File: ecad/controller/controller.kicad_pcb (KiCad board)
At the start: 2 copper layers, 48 x 30 mm, 43 parts, among them J2 USB_C_Receptacle_PowerOnly_6P, SW1 SW, SW2 SW, SW3 SW, U1 ESP32-S3-WROOM-1, U2 AMS1117-3.3, U3 SN74LVC1T45DBV, U4 USBLC6-2SC6

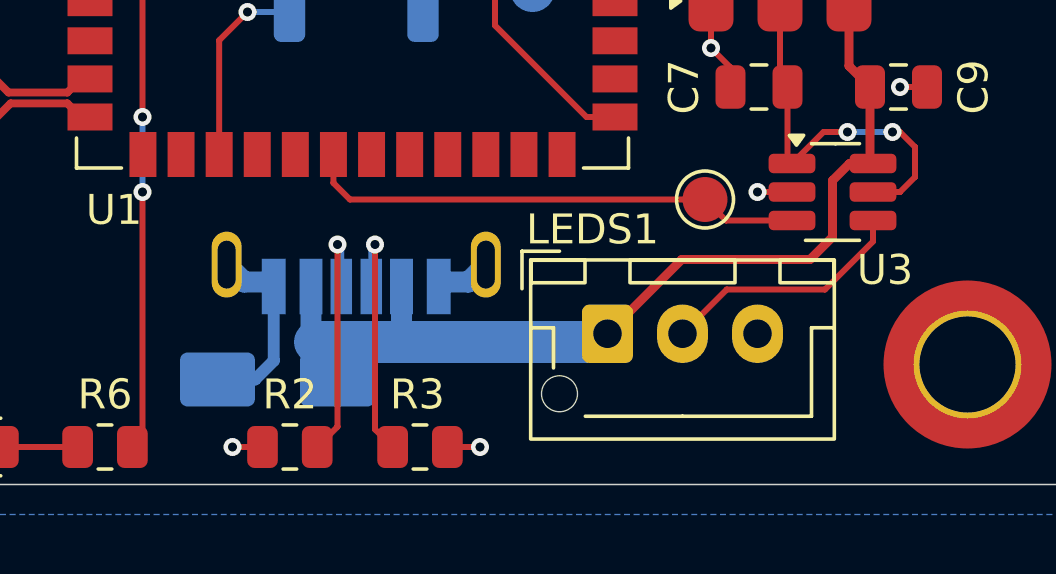
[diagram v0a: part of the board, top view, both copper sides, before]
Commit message: first controller board test complete! updated USB-C connector footprint as that was the only issue found so far
longer pads should make it easier to solder by giving the iron more clearance from the part; narrower shell mounting slots to reduce the sloppy fit and help alignment with 3D-printed casing
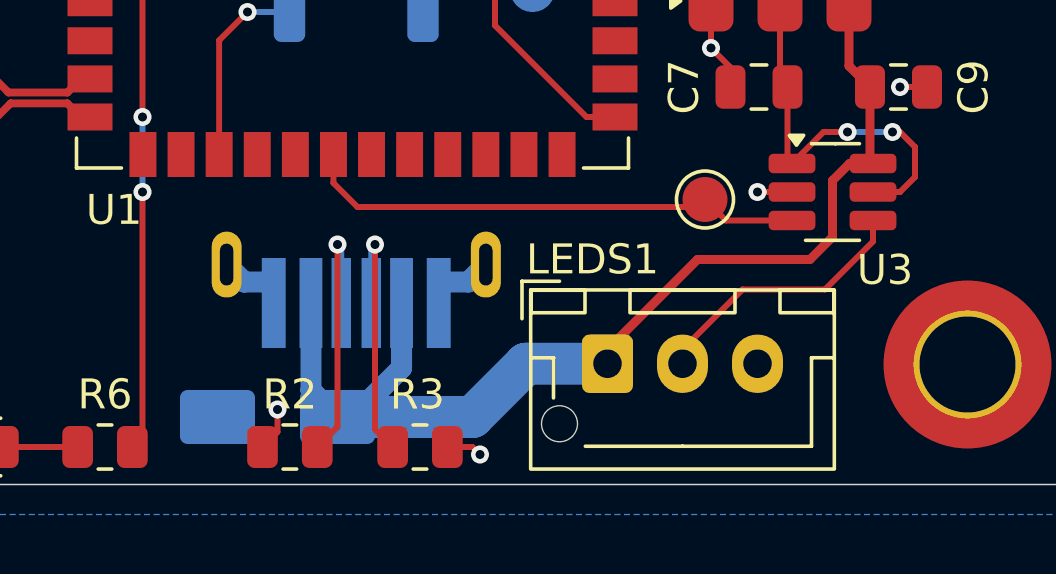
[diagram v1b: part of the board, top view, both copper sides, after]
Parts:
- moved D1 1.25 mm to (71.2, 62.5)
- moved LEDS1 1.00 mm to (82.2, 60.7)
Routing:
- net +5V: track 32.3 -> 37.6 mm
- net GND: track 31.0 -> 26.8 mm
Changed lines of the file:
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@@
 	(footprint "Connector_JST:JST_XH_B3B-XH-AM_1x03_P2.50mm_Vertical"
 		(layer "F.Cu")
-		(at 82.25 59.725)
+		(at 82.25 60.725)
 		(descr "JST XH series connector, B3B-XH-AM, with boss (http://www.jst-mfg.com/product/pdf/eng/eXH.pdf)")
 		(tags "connector JST XH vertical boss")
@@
 	(footprint "Diode_SMD:D_SMA"
 		(layer "B.Cu")
-		(at 71.25 61.25)
+		(at 71.25 62.5)
 		(descr "Diode SMA (DO-214AC)")
 		(tags "Diode SMA (DO-214AC)")
 		(property "Reference" "D1"
-			(at 0 2.5 0)
+			(at -2.75 -2.5 0)
 			(layer "B.SilkS")
 			(effects
@@
 		)
 		(pad "A5" smd rect
-			(at -0.5 -0.15 180)
-			(size 0.72 1.85)
+			(at -0.5 -0.7 180)
+			(size 0.65 3)
 			(layers "B.Cu" "B.Mask")
 			(net "Net-(J2-CC1)")
@@
 		)
 		(pad "A9" smd rect
-			(at 1.51 -0.15 180)
-			(size 0.76 1.85)
+			(at 1.51 -0.7 180)
+			(size 0.76 3)
 			(layers "B.Cu" "B.Mask")
 			(net "+5V")
@@
 		)
 		(pad "A12" smd rect
-			(at 2.75 -0.15 180)
-			(size 0.8 1.85)
+			(at 2.75 -0.7 180)
+			(size 0.8 3)
 			(layers "B.Cu" "B.Mask")
 			(net "GND")
@@
 		)
 		(pad "B5" smd rect
-			(at 0.5 -0.15 180)
-			(size 0.72 1.85)
+			(at 0.5 -0.7 180)
+			(size 0.65 3)
 			(layers "B.Cu" "B.Mask")
 			(net "Net-(J2-CC2)")
@@
 		)
 		(pad "B9" smd rect
-			(at -1.51 -0.15 180)
-			(size 0.76 1.85)
+			(at -1.51 -0.7 180)
+			(size 0.76 3)
 			(layers "B.Cu" "B.Mask")
 			(net "+5V")
@@
 		)
 		(pad "B12" smd rect
-			(at -2.75 -0.15 180)
-			(size 0.8 1.85)
+			(at -2.75 -0.7 180)
+			(size 0.8 3)
 			(layers "B.Cu" "B.Mask")
 			(net "GND")
@@
 			(at -4.32 0.58 180)
 			(size 1 2.2)
-			(drill oval 0.6 1.6)
+			(drill oval 0.45 1.4)
 			(property pad_prop_mechanical)
 			(layers "*.Cu" "*.Mask")
@@
 			(at 4.32 0.58 180)
 			(size 1 2.2)
-			(drill oval 0.6 1.6)
+			(drill oval 0.45 1.4)
 			(property pad_prop_mechanical)
 			(layers "*.Cu" "*.Mask")
@@
 	)
 	(segment
-		(start 76.9125 63.5)
-		(end 78 63.5)
+		(start 71.25 62.25)
+		(end 71.25 63)
 		(width 0.2)
 		(layer "F.Cu")
@@
 	)
 	(segment
-		(start 70.75 63.5)
-		(end 69.75 63.5)
+		(start 71.25 63)
+		(end 70.75 63.5)
 		(width 0.2)
 		(layer "F.Cu")
@@
 	)
 	(segment
+		(start 77.75 63.5)
+		(end 78 63.75)
+		(width 0.2)
+		(layer "F.Cu")
+		(net "GND")
+	)
+	(segment
 		(start 54.1 37.65)
 		(end 54.25 37.5)
@@
 	)
 	(segment
+		(start 76.9125 63.5)
+		(end 77.75 63.5)
+		(width 0.2)
+		(layer "F.Cu")
+		(net "GND")
+	)
+	(segment
 		(start 86.35 50.85)
 		(end 85.7 50.2)
@@
 	)
 	(via
-		(at 69.75 63.5)
+		(at 71.25 62.25)
 		(size 0.6)
 		(drill 0.3)
@@
 	)
 	(via
-		(at 78 63.5)
+		(at 78 63.75)
 		(size 0.6)
 		(drill 0.3)
@@
 	)
 	(segment
-		(start 69.25 61.25)
-		(end 70.5 61.25)
-		(width 0.4)
-		(layer "B.Cu")
-		(net "GND")
-	)
-	(segment
 		(start 70.135 58)
 		(end 69.555 57.42)
@@
 	)
 	(segment
-		(start 71.125 60.625)
-		(end 71.125 58)
-		(width 0.4)
-		(layer "B.Cu")
-		(net "GND")
-	)
-	(segment
-		(start 70.5 61.25)
-		(end 71.125 60.625)
-		(width 0.4)
-		(layer "B.Cu")
-		(net "GND")
-	)
-	(segment
 		(start 90.25 53)
 		(end 89.45 53)
@@
 	)
 	(segment
-		(start 84.725 57.25)
+		(start 85.25 57.25)
 		(end 89 57.25)
 		(width 0.3)
@@
 	)
 	(segment
-		(start 89 57.25)
-		(end 89.75 56.5)
+		(start 82.25 60.25)
+		(end 82.25 60.725)
 		(width 0.3)
 		(layer "F.Cu")
@@
 	)
 	(segment
-		(start 91 53.95)
-		(end 91.1 54.05)
+		(start 89.75 56.5)
+		(end 89.75 54.620001)
 		(width 0.3)
 		(layer "F.Cu")
@@
 	)
 	(segment
-		(start 82.25 59.725)
-		(end 84.725 57.25)
+		(start 91 53.95)
+		(end 91.1 54.05)
 		(width 0.3)
 		(layer "F.Cu")
@@
 	)
 	(segment
-		(start 82.525 59.725)
-		(end 82.25 59.725)
+		(start 89 57.25)
+		(end 89.75 56.5)
 		(width 0.3)
 		(layer "F.Cu")
@@
 	)
 	(segment
-		(start 89.75 56.5)
-		(end 89.75 54.620001)
+		(start 85.25 57.25)
+		(end 82.25 60.25)
 		(width 0.3)
 		(layer "F.Cu")
@@
 	)
 	(segment
-		(start 75.5 60)
-		(end 72.5 60)
+		(start 82.25 60.725)
+		(end 79.525 60.725)
 		(width 1.4)
 		(layer "B.Cu")
@@
 	)
 	(segment
-		(start 75.385 59.885)
-		(end 75.5 60)
+		(start 72.365 58.7)
+		(end 72.365 61.615)
 		(width 0.7)
 		(layer "B.Cu")
@@
 	)
 	(segment
-		(start 75.385 58)
-		(end 75.385 59.885)
+		(start 79.525 60.725)
+		(end 77.75 62.5)
+		(width 1.4)
+		(layer "B.Cu")
+		(net "+5V")
+	)
+	(segment
+		(start 73.75 62.5)
+		(end 73.25 62.5)
 		(width 0.7)
 		(layer "B.Cu")
@@
 	)
 	(segment
-		(start 72.365 59.865)
-		(end 72.5 60)
-		(width 0.2)
+		(start 72.365 61.615)
+		(end 73.25 62.5)
+		(width 0.7)
 		(layer "B.Cu")
 		(net "+5V")
 	)
 	(segment
-		(start 72.365 58)
-		(end 72.365 59.865)
+		(start 75.385 58.7)
+		(end 75.385 60.865)
 		(width 0.7)
 		(layer "B.Cu")
@@
 	)
 	(segment
-		(start 75.5 60)
-		(end 81.975 60)
-		(width 1.4)
+		(start 75.385 60.865)
+		(end 73.75 62.5)
+		(width 0.7)
 		(layer "B.Cu")
 		(net "+5V")
 	)
 	(segment
-		(start 81.975 60)
-		(end 82.25 59.725)
+		(start 77.75 62.5)
+		(end 73.25 62.5)
 		(width 1.4)
 		(layer "B.Cu")
@@
 	)
 	(segment
-		(start 86.2 55.95)
-		(end 88.4 55.95)
+		(start 73.115 53.75)
+		(end 73.115 54.7)
 		(width 0.2)
 		(layer "F.Cu")
@@
 	)
 	(segment
-		(start 73.115 53.75)
-		(end 73.115 54.7)
+		(start 86.2 55.95)
+		(end 88.4 55.95)
 		(width 0.2)
 		(layer "F.Cu")
@@
 	(segment
 		(start 73.115 54.7)
-		(end 73.665 55.25)
+		(end 73.915 55.5)
 		(width 0.2)
 		(layer "F.Cu")
@@
 	)
 	(segment
-		(start 85.5 55.25)
-		(end 86.2 55.95)
+		(start 85.25 55.5)
+		(end 85.5 55.25)
 		(width 0.2)
 		(layer "F.Cu")
@@
 	)
 	(segment
-		(start 73.665 55.25)
-		(end 85.5 55.25)
+		(start 85.5 55.25)
+		(end 86.2 55.95)
 		(width 0.2)
 		(layer "F.Cu")
@@
 	)
 	(segment
-		(start 91.1 55.95)
-		(end 91.1 56.65)
+		(start 73.915 55.5)
+		(end 85.25 55.5)
 		(width 0.2)
 		(layer "F.Cu")
-		(net "/LED_SIG")
+		(net "/LED_GPIO")
 	)
 	(segment
-		(start 84.75 59.5875)
-		(end 84.75 59.725)
+		(start 91.1 56.65)
+		(end 91.1 55.95)
 		(width 0.2)
 		(layer "F.Cu")
@@
 	)
 	(segment
-		(start 91.1 56.65)
+		(start 86.75 58.25)
 		(end 89.5 58.25)
 		(width 0.2)
@@
 	)
 	(segment
-		(start 86.225 58.25)
-		(end 84.75 59.725)
+		(start 84.75 60.25)
+		(end 86.75 58.25)
 		(width 0.2)
 		(layer "F.Cu")
@@
 	(segment
 		(start 89.5 58.25)
-		(end 86.225 58.25)
+		(end 91.1 56.65)
 		(width 0.2)
 		(layer "F.Cu")
